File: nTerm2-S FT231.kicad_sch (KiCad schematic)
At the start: 126 parts, among them J1 VGA, J2 Keyboard, J3 Mouse, J4 Line-out/Speaker, J5 RS-232 V.24, J6 USB_C_Receptacle_USB2.0_16P, J7 Line-out/Speaker, K1 IM41 3V, K2 IM41 3V, K3 IM41 3V, Q1 BC817, Q2 BC817, Q3 BC817, Q4 BC817, Q5 BC817, Q6 BC817, Q7 BC817, Q8 BC817, SW1 IO0, SW2 RESET, SW3 DEFAULTS, U1 ESP32-WROOM-32, U2 LM386, U3 MAX3232E, U4 DS2417, U5 NCP1117-3.3_SOT223, U6 USBLC6-2SC6, U7 FT231XS, Y1 32.768MHz

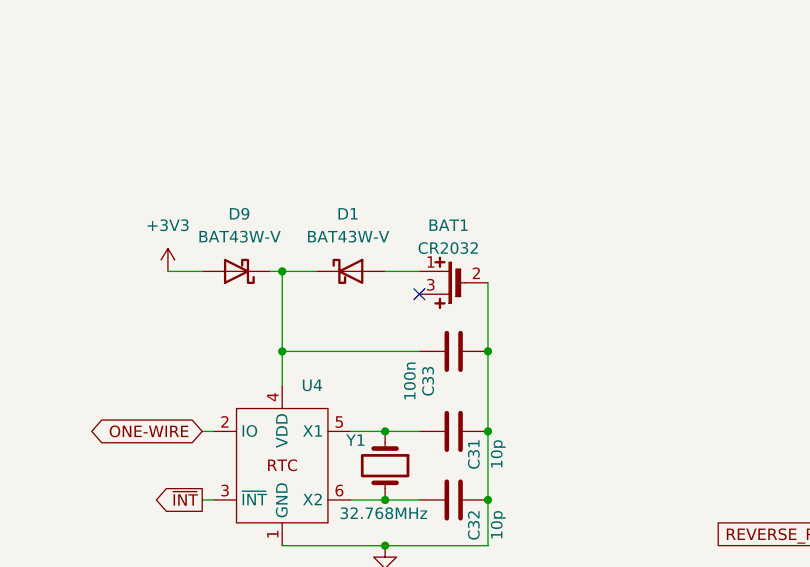
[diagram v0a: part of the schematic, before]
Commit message: V0.10 small detail fixes. - Rotate C19 180 degrees, so that it's oriented as the rest of the caps. - Tweak the positions of several connectors and LEDs so that they are flush with the PCB edge. - Connect pins 2 and 3 (both +) of the battery housing together so that it doesn't matter anymore to which hole you solder the + wire.
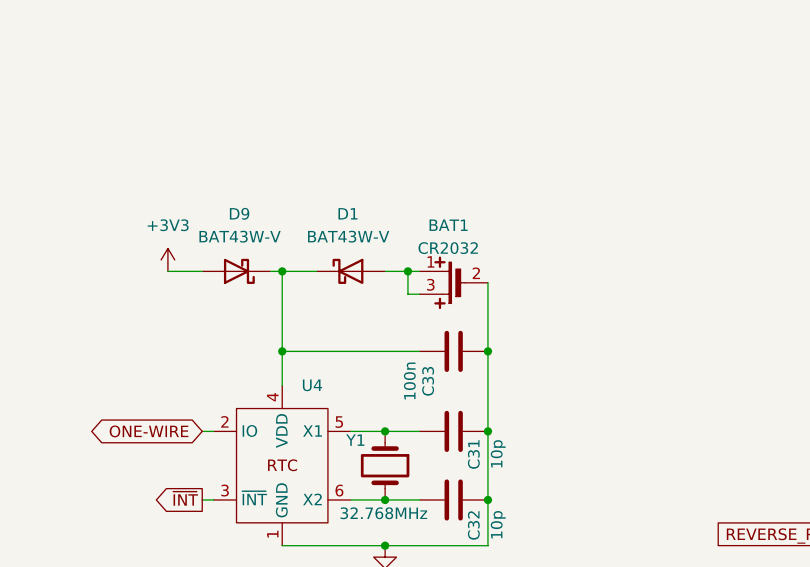
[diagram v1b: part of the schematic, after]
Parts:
- BAT1: footprint Sporos_Tech_Footprints:TE Connectivity CR2032 V -> nTerm2-S:TE Connectivity CR2032 V
- J1: footprint Sporos_Tech_Footprints:DSUB-15-HD AssMann HD 15FW -> 'nTerm2-S:DSUB-15-HD AssMann HD 15FW
- J5: footprint Connector_Dsub:DSUB-9_Pins_Horizontal_P2.77x2.84mm_EdgePinOffset7.70mm_Housed_MountingHolesOffset9.12mm -> nTerm2-S:DSUB-9_Pins_Horizontal_P2.77x2.84mm_EdgePinOffset7.70mm_Housed_MountingHolesOffset9.12mm
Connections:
- net at BAT1.1, D1.2 (A): now also BAT1.3
- no-connect marks 26 -> 25
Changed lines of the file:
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@@
 	(title_block
 		(title "nTerm2-s")
-		(date "2025-06-05")
-		(rev "0.09")
+		(date "2025-06-23")
+		(rev "0.10")
 		(company "Sporos Tech ₍^•_•^₎ﾉ")
 		(comment 1 "Peter de Vroomen")
@@
 	)
 	(junction
+		(at 259.08 168.91)
+		(diameter 0)
+		(color 0 0 0 0)
+	)
+	(junction
 		(at 351.79 220.98)
 		(diameter 0)
@@
 	)
 	(no_connect
-		(at 260.35 171.45)
-	)
-	(no_connect
 		(at 321.31 119.38)
 	)
@@
 	(wire
 		(pts
+			(xy 259.08 168.91) (xy 259.08 171.45)
+		)
+		(stroke
+			(width 0)
+			(type default)
+		)
+	)
+	(wire
+		(pts
 			(xy 147.32 163.83) (xy 146.05 163.83)
 		)
@@
 	(wire
 		(pts
+			(xy 259.08 168.91) (xy 260.35 168.91)
+		)
+		(stroke
+			(width 0)
+			(type default)
+		)
+	)
+	(wire
+		(pts
 			(xy 193.04 176.53) (xy 199.39 176.53)
 		)
@@
 	(wire
 		(pts
+			(xy 260.35 171.45) (xy 259.08 171.45)
+		)
+		(stroke
+			(width 0)
+			(type default)
+		)
+	)
+	(wire
+		(pts
 			(xy 252.73 186.69) (xy 256.54 186.69)
 		)
@@
 	(wire
 		(pts
-			(xy 256.54 168.91) (xy 260.35 168.91)
+			(xy 256.54 168.91) (xy 259.08 168.91)
 		)
 		(stroke
@@
 			)
 		)
-		(property "Footprint" "Sporos_Tech_Footprints:DSUB-15-HD AssMann HD 15FW"
+		(property "Footprint" "'nTerm2-S:DSUB-15-HD AssMann HD 15FW"
 			(at 332.74 35.56 0)
 			(effects
@@
 			)
 		)
-		(property "Footprint" "Connector_Dsub:DSUB-9_Pins_Horizontal_P2.77x2.84mm_EdgePinOffset7.70mm_Housed_MountingHolesOffset9.12mm"
+		(property "Footprint" "nTerm2-S:DSUB-9_Pins_Horizontal_P2.77x2.84mm_EdgePinOffset7.70mm_Housed_MountingHolesOffset9.12mm"
 			(at 224.79 240.03 0)
 			(effects
@@
 			)
 		)
-		(property "Footprint" "Sporos_Tech_Footprints:TE Connectivity CR2032 V"
+		(property "Footprint" "nTerm2-S:TE Connectivity CR2032 V"
 			(at 264.16 170.18 0)
 			(effects

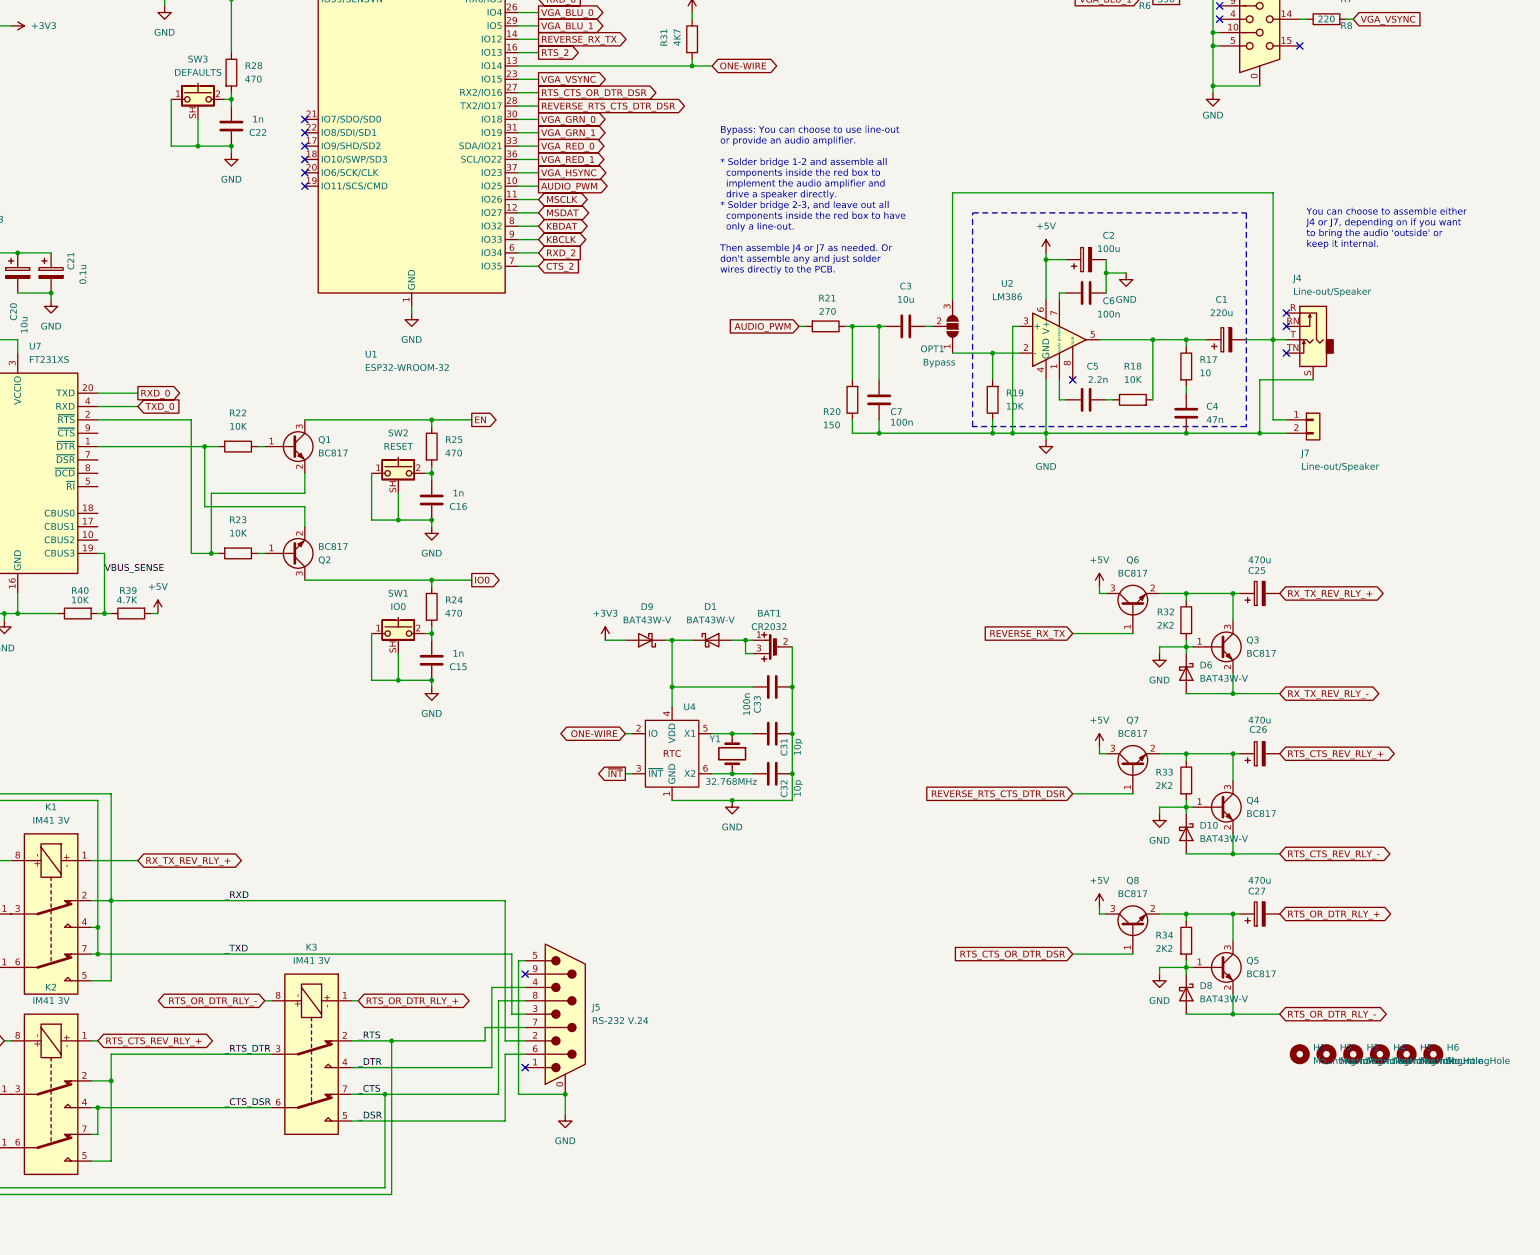
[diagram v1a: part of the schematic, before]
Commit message: nTerm2-S V0.11
* Added a footprint for a volume control potmeter.
* Improved routing around R29, R26, R43 and R31. It's not super still, but better than routing 2 traces under a resistor.
* New documentation, including a proper render that will help with placing components.
* Added bunch of 3D packages
* Resolved some library issues
* Created fabrication files for v0.11
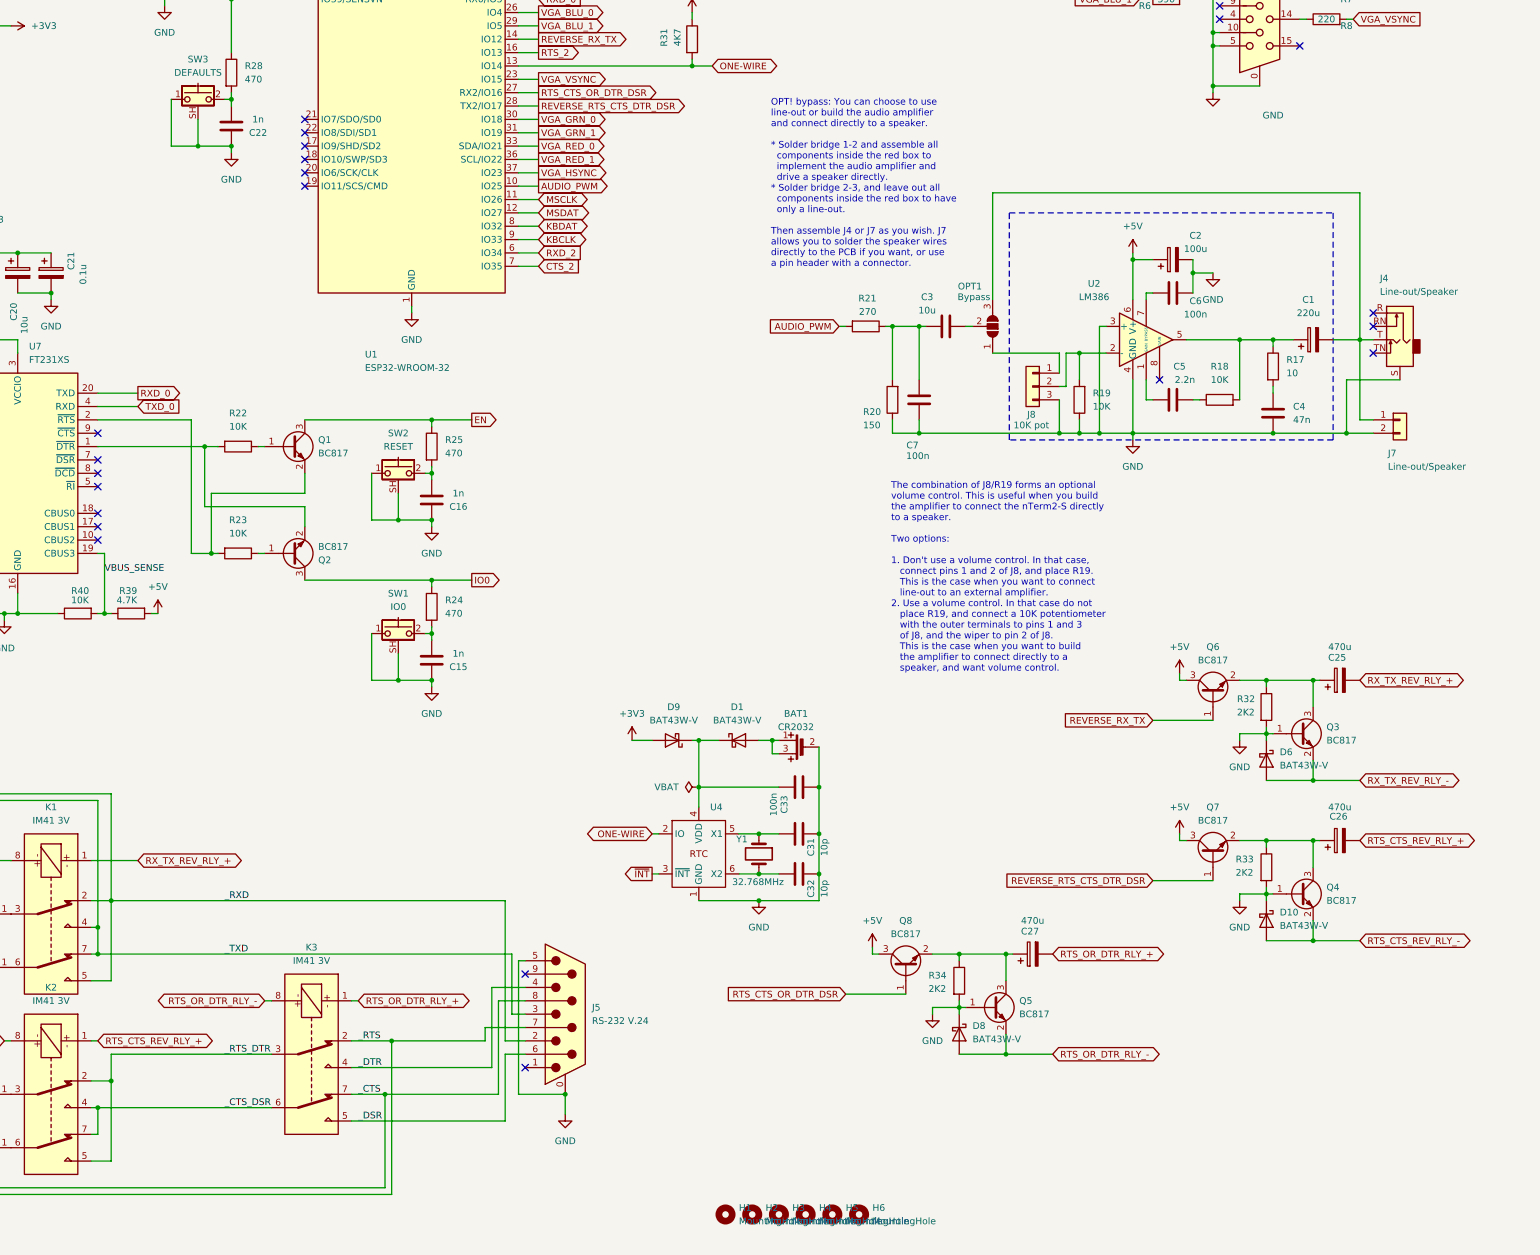
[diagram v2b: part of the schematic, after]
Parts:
- added J8: 10K pot, Connector_PinHeader_2.54mm:PinHeader_1x03_P2.54mm_Vertical, symbol Connector_Generic:Conn_01x03
- C1, C25, C26, C27: footprint Library:CP_Elec_6.3x7.7 -> nTerm2-S:CP_Elec_6.3x7.7
- C10, C11, C12, C14, C17, C19, C21, C8, C9: footprint Library:CP_EIA-3216-18_Kemet-A_Pad1.58x1.35mm_HandSolder -> nTerm2-S:CP_EIA-3216-18_Kemet-A_Pad1.58x1.35mm_HandSolder
- C13, C18: footprint Library:CP_EIA-6032-28_Kemet-C_Pad2.25x2.35mm_HandSolder -> nTerm2-S:CP_EIA-6032-28_Kemet-C_Pad2.25x2.35mm_HandSolder
- C15, C16, C22, C24, C28, C29, C30, C31, C32, C33, C4, C5, C6, C7: footprint Library:C_0603_1608Metric_Pad1.08x0.95mm_HandSolder -> nTerm2-S:C_0603_1608Metric_Pad1.08x0.95mm_HandSolder
- C2: footprint Library:CP_Elec_5x5.4 -> nTerm2-S:CP_Elec_5x5.4
- C20: footprint Library:CP_EIA-3528-21_Kemet-B_Pad1.50x2.35mm_HandSolder -> nTerm2-S:CP_EIA-3528-21_Kemet-B_Pad1.50x2.35mm_HandSolder
- C23: footprint Library:CP_EIA-7343-30_AVX-N_Pad2.25x2.55mm_HandSolder -> nTerm2-S:CP_EIA-7343-30_AVX-N_Pad2.25x2.55mm_HandSolder
- C3: footprint Library:C_0805_2012Metric_Pad1.18x1.45mm_HandSolder -> nTerm2-S:C_0805_2012Metric_Pad1.18x1.45mm_HandSolder
- D1, D10, D6, D8, D9: footprint Library:D_SOD-123 -> nTerm2-S:D_SOD-123
- D11, D12: footprint Library:DIALIGHT_LED_3MM_DOUBLE -> nTerm2-S:DIALIGHT_LED_3MM_DOUBLE
- D3: footprint Library:Nexperia_CFP3_SOD-123W -> nTerm2-S:Nexperia_CFP3_SOD-123W
- D4: footprint Library:DIALIGHT_LED_3MM_SINGLE -> nTerm2-S:DIALIGHT_LED_3MM_SINGLE
- H1, H2, H3, H4, H5, H6: footprint Library:MountingHole_3.2mm_M3 -> nTerm2-S:MountingHole_3.2mm_M3
- J1: footprint 'nTerm2-S:DSUB-15-HD AssMann HD 15FW -> nTerm2-S:DSUB-15-HD AssMann HD 15FW
- J2, J3: footprint Library:Connector_Mini-DIN_Female_6Pin_2rows -> nTerm2-S:Connector_Mini-DIN_Female_6Pin_2rows
- J4: footprint Library:Jack_3.5mm_Ledino_KB3SPRS_Horizontal-alt -> nTerm2-S:Jack_3.5mm_Ledino_KB3SPRS_Horizontal-alt
- J6: footprint Library:USB_C_Receptacle_Molex_213716-0001 -> nTerm2-S:USB_C_Receptacle_Molex_213716-0001
- J7: footprint Library:PinHeader_1x02_P2.54mm_Vertical -> nTerm2-S:PinHeader_1x02_P2.54mm_Vertical
- K1, K2, K3: footprint Library:Relay_DPDT_AXICOM_IMSeries_Gullwing -> nTerm2-S:Relay_DPDT_AXICOM_IMSeries_Gullwing
- OPT1, OPT2, OPT3, OPT4, OPT5: footprint Library:SolderJumper-3_P1.3mm_Open_RoundedPad1.0x1.5mm_NumberLabels -> nTerm2-S:SolderJumper-3_P1.3mm_Open_RoundedPad1.0x1.5mm_NumberLabels
- Q1, Q2, Q3, Q4, Q5, Q6, Q7, Q8: footprint Library:SOT-23 -> nTerm2-S:SOT-23
- R1, R10, R11, R12, R13, R14, R15, R16, R17, R18, R19, R2, R20, R21, R22, R23, R24, R25, R26, R27, R28, R29, R3, R30, R31, R32, R33, R34, R35, R36, R37, R38, R39, R4, R40, R41, R42, R43, R5, R6, R7, R8, R9: footprint Library:R_0603_1608Metric_Pad0.98x0.95mm_HandSolder -> nTerm2-S:R_0603_1608Metric_Pad0.98x0.95mm_HandSolder
- SW1, SW2, SW3: footprint Library:SW_Tactile_SPST_Angled_PTS645Vx58-2LFS-alt -> nTerm2-S:SW_Tactile_SPST_Angled_PTS645Vx58-2LFS-alt
- U1: footprint Library:ESP32-WROOM-32 -> nTerm2-S:ESP32-WROOM-32
- U2: footprint Library:SOIC-8_3.9x4.9mm_P1.27mm -> nTerm2-S:SOIC-8_3.9x4.9mm_P1.27mm
- U3: footprint Library:SOIC-16_3.9x9.9mm_P1.27mm -> nTerm2-S:SOIC-16_3.9x9.9mm_P1.27mm
- U4: footprint Library:TSOC-6_3.76x3.94mm_P1.27mm -> nTerm2-S:TSOC-6_3.76x3.94mm_P1.27mm
- U5: footprint Library:SOT-223-3_TabPin2 -> nTerm2-S:SOT-223-3_TabPin2
- U6: footprint Library:SOT-23-6 -> nTerm2-S:SOT-23-6
- U7: footprint Library:SSOP-20_3.9x8.7mm_P0.635mm -> nTerm2-S:SSOP-20_3.9x8.7mm_P0.635mm
- Y1: footprint Library:Crystal_C38-LF_D3.0mm_L8.0mm_Horizontal -> nTerm2-S:Crystal_C38-LF_D3.0mm_L8.0mm_Horizontal
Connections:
- net GND: now also J8.3 (Pin_3)
- net at R19.2, U2.2 (-): now also J8.2 (Pin_2); no longer OPT1.1 (A)
- new net: J8.1 (Pin_1), OPT1.1 (A)
- no-connect marks 25 -> 32
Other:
- note added: "OPT! bypass: You can choose to use line-out or build the audio amplifier and connect directly to a speaker. * Solder bridge 1-2 and assemble all components inside the red box to implement the audio amplifier and drive a speaker directly. * Solder bridge 2-3, and leave out all components inside the red box to have only a line-out. Then assemble J4 or J7 as you wish. J7 allows you to solder the spe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"
- note added: "The combination of J8/R19 forms an optional volume control. This is useful when you build the amplifier to connect the nTerm2-S directly to a speaker. Two options: 1. Don't use a volume control. In that case, connect pins 1 and 2 of J8, and place R19. This is the case when you want to connect line-out to an external amplifier. 2. Use a volume control. In that case do not place R19, and connect a 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"
- note removed: "Bypass: You can choose to use line-out or provide an audio amplifier. * Solder bridge 1-2 and assemble all components inside the red box to implement the audio amplifier and drive a speaker directly. * Solder bridge 2-3, and leave out all components inside the red box to have only a line-out. Then assemble J4 or J7 as needed. Or don't assemble any and just solder wires directly to the PCB."
- note removed: "You can choose to assemble either J4 or J7, depending on if you want to bring the audio 'outside' or keep it internal."
- moved on the sheet: BAT1, C1, C2, C25, C26, C27, C3, C31, C32, C33, C4, C5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
